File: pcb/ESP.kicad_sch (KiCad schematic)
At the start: 6 parts, among them U5 ESP32-WROOM-32D

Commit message: poprawiony schemat w pdf
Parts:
- added C5, C6: 0.1uF/4VDC, Capacitor_SMD:C_0603_1608Metric, symbol Device:C
- added J10: Conn_01x06_Pin, Connector_PinHeader_2.54mm:PinHeader_1x06_P2.54mm_Vertical, symbol Connector:Conn_01x06_Pin
- added J14: Conn_02x05_Odd_Even, Connector_PinHeader_2.54mm:PinHeader_2x05_P2.54mm_Vertical, symbol Connector_Generic:Conn_02x05_Odd_Even
- added Q3, Q4: SS8050, Package_TO_SOT_SMD:SOT-23, symbol Transistor_BJT:SS8050
- added R1, R16: 10K, Resistor_SMD:R_0603_1608Metric, symbol Device:R
- added S1, S2: PTS636_SK25F_SMTR_LFS, 1bmoje:PTS636SK25FSMTRLFS, symbol Switch:SW_Push
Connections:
- net +3.3V: now also J10.1 (Pin_1), J14.1 (Pin_1)
- net EN: now also C6.2, Q3.3 (C), S2.2
- net GND: now also C5.1, C6.1, J10.2 (Pin_2), J14.10 (Pin_10), J14.3 (Pin_3), J14.5 (Pin_5), J14.9 (Pin_9), S1.1, S2.1
- net IO0: now also C5.2, Q4.3 (C), S1.2
- net IO12 renamed MTDI
- net MTDI: now also J14.8 (Pin_8)
- net IO13 renamed MTCK
- net MTCK: now also J14.4 (Pin_4)
- net IO14 renamed MTMS
- net MTMS: now also J14.2 (Pin_2)
- net IO15 renamed MTDO
- net MTDO: now also J14.6 (Pin_6)
- net IO16 renamed UART_PROGRAM_RXD
- net UART_PROGRAM_RXD: now also J10.3 (Pin_3)
- net IO17 renamed UART_PROGRAM_TXD
- net UART_PROGRAM_TXD: now also J10.4 (Pin_4)
- new net: Q4.1 (B), R16.2
- new net: Q3.1 (B), R1.2
- new net UART_PROGRAM_DTR: J10.5 (Pin_5), Q4.2 (E), R1.1
- new net UART_PROGRAM_RTS: J10.6 (Pin_6), Q3.2 (E), R16.1
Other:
- note added: "Buttons for RESET and programming"
- note added: "For programming"
- note added: "JTAG"
- note added: "UART for programming"
- moved on the sheet: C11, C12, C13, D1, R17, U5

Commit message: PCB poprawione
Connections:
- no-connect marks 0 -> 11

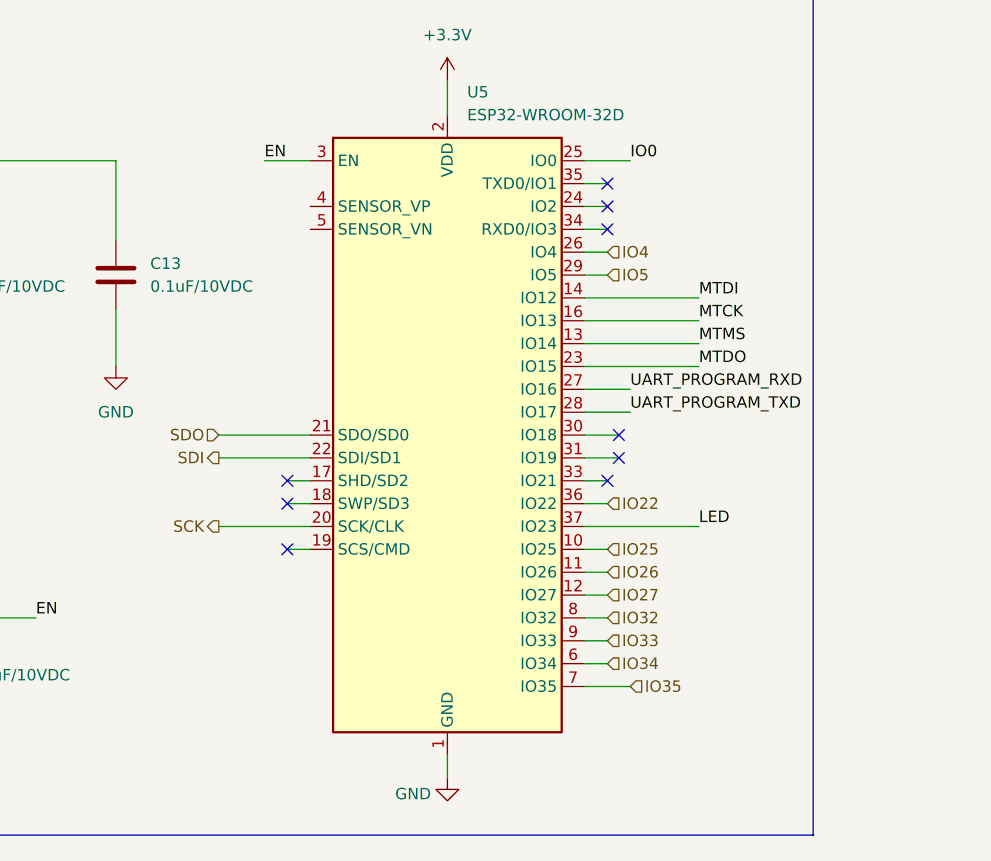
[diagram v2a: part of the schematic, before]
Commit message: PCB jeszcze mniejsza wersja
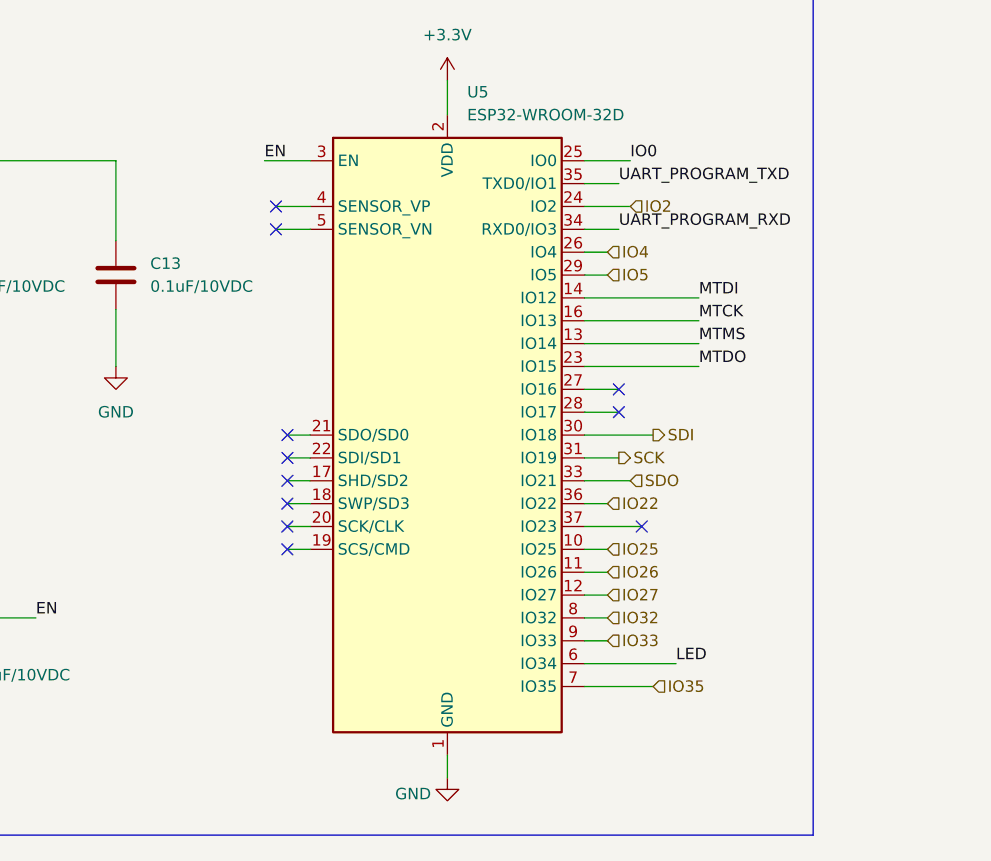
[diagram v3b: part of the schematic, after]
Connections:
- net IO34 is gone; now on net LED: U5.6 (IO34)
- net LED: no longer U5.37 (IO23)
- net SCK: now also U5.31 (IO19); no longer U5.20 (SCK/CLK)
- net SDI: now also U5.30 (IO18); no longer U5.22 (SDI/SD1)
- net SDO: now also U5.33 (IO21); no longer U5.21 (SDO/SD0)
- net UART_PROGRAM_RXD: now also U5.34 (RXD0/IO3); no longer U5.27 (IO16)
- net UART_PROGRAM_TXD: now also U5.35 (TXD0/IO1); no longer U5.28 (IO17)
- net IO2: now reaches U5.24 (IO2)
- no-connect marks 11 -> 13
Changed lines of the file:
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@@
 	)
 	(no_connect
-		(at 194.31 90.17)
+		(at 196.85 100.33)
+	)
+	(no_connect
+		(at 194.31 87.63)
+	)
+	(no_connect
+		(at 156.21 67.31)
+	)
+	(no_connect
+		(at 157.48 92.71)
+	)
+	(no_connect
+		(at 157.48 97.79)
 	)
 	(no_connect
@@
 	)
 	(no_connect
-		(at 193.04 67.31)
+		(at 157.48 95.25)
 	)
 	(no_connect
-		(at 193.04 95.25)
+		(at 157.48 100.33)
 	)
 	(no_connect
-		(at 193.04 62.23)
+		(at 157.48 90.17)
 	)
 	(no_connect
-		(at 194.31 92.71)
+		(at 194.31 85.09)
 	)
 	(no_connect
-		(at 157.48 95.25)
-	)
-	(no_connect
-		(at 193.04 64.77)
+		(at 156.21 64.77)
 	)
 	(no_connect
@@
 	)
 	(no_connect
-		(at 157.48 97.79)
-	)
-	(no_connect
 		(at 271.78 40.64)
 	)
@@
 	(wire
 		(pts
-			(xy 190.5 118.11) (xy 195.58 118.11)
-		)
-		(stroke
-			(width 0)
-			(type default)
-		)
-	)
-	(wire
-		(pts
 			(xy 190.5 92.71) (xy 194.31 92.71)
 		)
@@
 	(wire
 		(pts
-			(xy 190.5 87.63) (xy 195.58 87.63)
-		)
-		(stroke
-			(width 0)
-			(type default)
-		)
-	)
-	(wire
-		(pts
-			(xy 190.5 90.17) (xy 194.31 90.17)
+			(xy 190.5 90.17) (xy 198.12 90.17)
 		)
 		(stroke
@@
 	(wire
 		(pts
-			(xy 190.5 100.33) (xy 203.2 100.33)
-		)
-		(stroke
-			(width 0)
-			(type default)
-		)
-	)
-	(wire
-		(pts
 			(xy 58.42 143.51) (xy 62.23 143.51)
 		)
@@
 	(wire
 		(pts
-			(xy 149.86 100.33) (xy 160.02 100.33)
-		)
-		(stroke
-			(width 0)
-			(type default)
-		)
-	)
-	(wire
-		(pts
 			(xy 118.11 59.69) (xy 138.43 59.69)
 		)
@@
 	(wire
 		(pts
+			(xy 160.02 90.17) (xy 157.48 90.17)
+		)
+		(stroke
+			(width 0)
+			(type default)
+		)
+	)
+	(wire
+		(pts
 			(xy 69.85 83.82) (xy 69.85 95.25)
 		)
@@
 	(wire
 		(pts
+			(xy 190.5 118.11) (xy 198.12 118.11)
+		)
+		(stroke
+			(width 0)
+			(type default)
+		)
+	)
+	(wire
+		(pts
 			(xy 190.5 102.87) (xy 193.04 102.87)
 		)
@@
 	(wire
 		(pts
+			(xy 194.31 85.09) (xy 190.5 85.09)
+		)
+		(stroke
+			(width 0)
+			(type default)
+		)
+	)
+	(wire
+		(pts
 			(xy 246.38 127) (xy 246.38 128.27)
 		)
@@
 	(wire
 		(pts
-			(xy 190.5 115.57) (xy 193.04 115.57)
+			(xy 194.31 87.63) (xy 190.5 87.63)
 		)
 		(stroke
@@
 	(wire
 		(pts
+			(xy 160.02 95.25) (xy 157.48 95.25)
+		)
+		(stroke
+			(width 0)
+			(type default)
+		)
+	)
+	(wire
+		(pts
 			(xy 46.99 86.36) (xy 48.26 86.36)
 		)
@@
 	(wire
 		(pts
-			(xy 190.5 85.09) (xy 195.58 85.09)
-		)
-		(stroke
-			(width 0)
-			(type default)
-		)
-	)
-	(wire
-		(pts
 			(xy 58.42 140.97) (xy 60.96 140.97)
 		)
@@
 	(wire
 		(pts
-			(xy 190.5 64.77) (xy 193.04 64.77)
-		)
-		(stroke
-			(width 0)
-			(type default)
-		)
-	)
-	(wire
-		(pts
-			(xy 160.02 95.25) (xy 157.48 95.25)
+			(xy 190.5 64.77) (xy 195.58 64.77)
 		)
 		(stroke
@@
 	(wire
 		(pts
+			(xy 156.21 67.31) (xy 160.02 67.31)
+		)
+		(stroke
+			(width 0)
+			(type default)
+		)
+	)
+	(wire
+		(pts
 			(xy 246.38 96.52) (xy 246.38 105.41)
 		)
@@
 	(wire
 		(pts
-			(xy 149.86 90.17) (xy 160.02 90.17)
-		)
-		(stroke
-			(width 0)
-			(type default)
-		)
-	)
-	(wire
-		(pts
 			(xy 72.39 40.64) (xy 72.39 45.72)
 		)
@@
 	(wire
 		(pts
-			(xy 190.5 67.31) (xy 193.04 67.31)
+			(xy 157.48 92.71) (xy 160.02 92.71)
 		)
 		(stroke
@@
 	(wire
 		(pts
+			(xy 190.5 62.23) (xy 194.31 62.23)
+		)
+		(stroke
+			(width 0)
+			(type default)
+		)
+	)
+	(wire
+		(pts
 			(xy 46.99 88.9) (xy 48.26 88.9)
 		)
@@
 	(wire
 		(pts
+			(xy 156.21 64.77) (xy 160.02 64.77)
+		)
+		(stroke
+			(width 0)
+			(type default)
+		)
+	)
+	(wire
+		(pts
+			(xy 190.5 115.57) (xy 200.66 115.57)
+		)
+		(stroke
+			(width 0)
+			(type default)
+		)
+	)
+	(wire
+		(pts
+			(xy 190.5 67.31) (xy 194.31 67.31)
+		)
+		(stroke
+			(width 0)
+			(type default)
+		)
+	)
+	(wire
+		(pts
 			(xy 118.11 76.2) (xy 118.11 82.55)
 		)
@@
 	(wire
 		(pts
+			(xy 160.02 97.79) (xy 157.48 97.79)
+		)
+		(stroke
+			(width 0)
+			(type default)
+		)
+	)
+	(wire
+		(pts
 			(xy 160.02 102.87) (xy 157.48 102.87)
 		)
@@
 	(wire
 		(pts
-			(xy 190.5 62.23) (xy 193.04 62.23)
-		)
-		(stroke
-			(width 0)
-			(type default)
-		)
-	)
-	(wire
-		(pts
 			(xy 190.5 74.93) (xy 203.2 74.93)
 		)
@@
 	(wire
 		(pts
-			(xy 160.02 97.79) (xy 157.48 97.79)
-		)
-		(stroke
-			(width 0)
-			(type default)
-		)
-	)
-	(wire
-		(pts
 			(xy 45.72 40.64) (xy 72.39 40.64)
 		)
@@
 	(wire
 		(pts
-			(xy 190.5 95.25) (xy 193.04 95.25)
+			(xy 190.5 95.25) (xy 195.58 95.25)
 		)
 		(stroke
@@
 	(wire
 		(pts
-			(xy 149.86 92.71) (xy 160.02 92.71)
-		)
-		(stroke
-			(width 0)
-			(type default)
-		)
-	)
-	(wire
-		(pts
 			(xy 45.72 33.02) (xy 48.26 33.02)
+		)
+		(stroke
+			(width 0)
+			(type default)
+		)
+	)
+	(wire
+		(pts
+			(xy 190.5 100.33) (xy 196.85 100.33)
+		)
+		(stroke
+			(width 0)
+			(type default)
+		)
+	)
+	(wire
+		(pts
+			(xy 160.02 100.33) (xy 157.48 100.33)
 		)
 		(stroke
@@
 	)
 	(label "UART_PROGRAM_TXD"
-		(at 195.58 87.63 0)
+		(at 194.31 62.23 0)
 		(effects
 			(font
@@
 	)
 	(label "UART_PROGRAM_RXD"
-		(at 195.58 85.09 0)
+		(at 194.31 67.31 0)
 		(effects
 			(font
@@
 	)
 	(label "LED"
-		(at 203.2 100.33 0)
+		(at 200.66 115.57 0)
 		(effects
 			(font
@@
 	(hierarchical_label "SCK"
 		(shape output)
-		(at 149.86 100.33 180)
-		(effects
-			(font
-				(size 1.27 1.27)
-			)
-			(justify right)
+		(at 194.31 92.71 0)
+		(effects
+			(font
+				(size 1.27 1.27)
+			)
+			(justify left)
 		)
 	)
 	(hierarchical_label "SDI"
 		(shape output)
-		(at 149.86 92.71 180)
-		(effects
-			(font
-				(size 1.27 1.27)
-			)
-			(justify right)
+		(at 198.12 90.17 0)
+		(effects
+			(font
+				(size 1.27 1.27)
+			)
+			(justify left)
 		)
 	)
@@
 	(hierarchical_label "SDO"
 		(shape input)
-		(at 149.86 90.17 180)
-		(effects
-			(font
-				(size 1.27 1.27)
-			)
-			(justify right)
-		)
-	)
-	(hierarchical_label "IO35"
+		(at 195.58 95.25 0)
+		(effects
+			(font
+				(size 1.27 1.27)
+			)
+			(justify left)
+		)
+	)
+	(hierarchical_label "IO2"
 		(shape input)
-		(at 195.58 118.11 0)
+		(at 195.58 64.77 0)
 		(effects
 			(font
@@
 		)
 	)
-	(hierarchical_label "IO34"
+	(hierarchical_label "IO35"
 		(shape input)
-		(at 193.04 115.57 0)
-		(effects
-			(font
+		(at 198.12 118.11 0)
+		(effects
+			(font

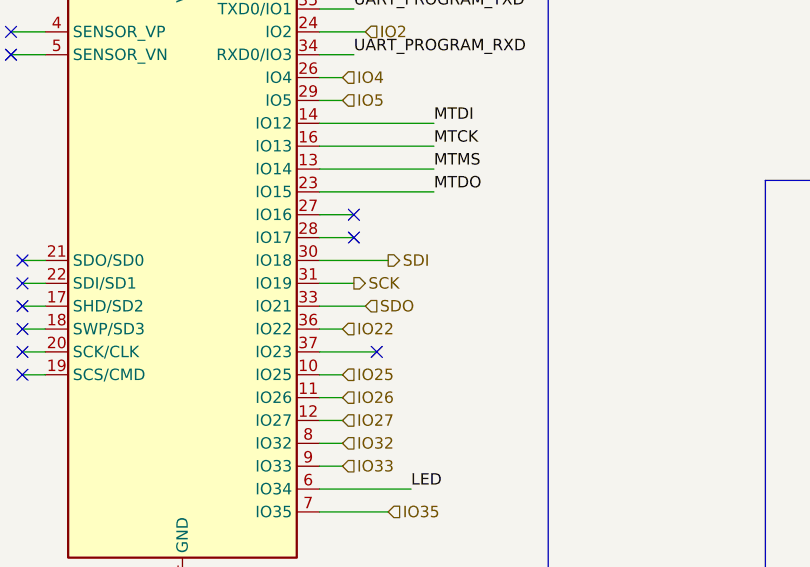
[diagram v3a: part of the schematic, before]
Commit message: 4 layer PCB
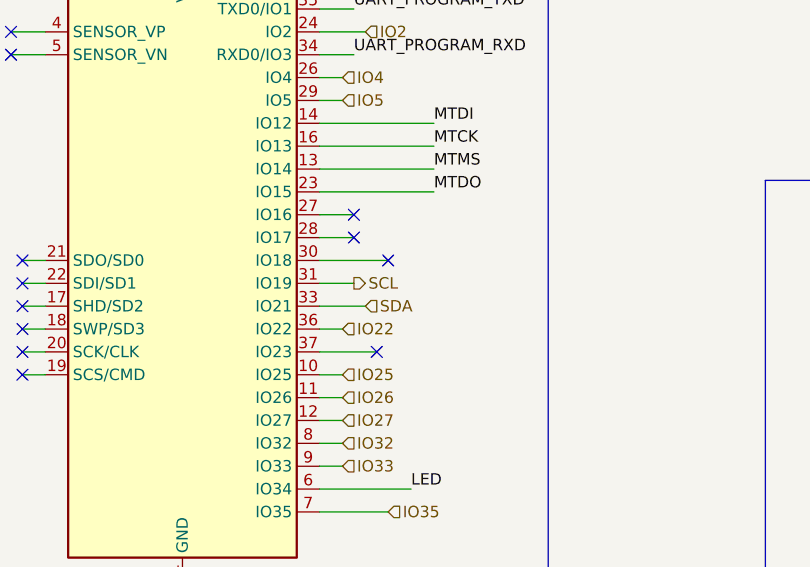
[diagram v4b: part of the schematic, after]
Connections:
- net SCK renamed SCL
- net SDI: no longer names the net of U5.30 (IO18)
- net SDO renamed SDA
- no-connect marks 13 -> 14
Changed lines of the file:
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@@
+	)
+	(no_connect
+		(at 198.12 90.17)
 	)
 	(no_connect
@@
 		)
 	)
-	(hierarchical_label "SCK"
+	(hierarchical_label "SCL"
 		(shape output)
 		(at 194.31 92.71 0)
-		(effects
-			(font
-				(size 1.27 1.27)
-			)
-			(justify left)
-		)
-	)
-	(hierarchical_label "SDI"
-		(shape output)
-		(at 198.12 90.17 0)
 		(effects
 			(font
@@
 		)
 	)
-	(hierarchical_label "SDO"
+	(hierarchical_label "SDA"
 		(shape input)
 		(at 195.58 95.25 0)
